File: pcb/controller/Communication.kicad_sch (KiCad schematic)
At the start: 4 parts, among them U2 SP3485EN, U3 E220-400M22S

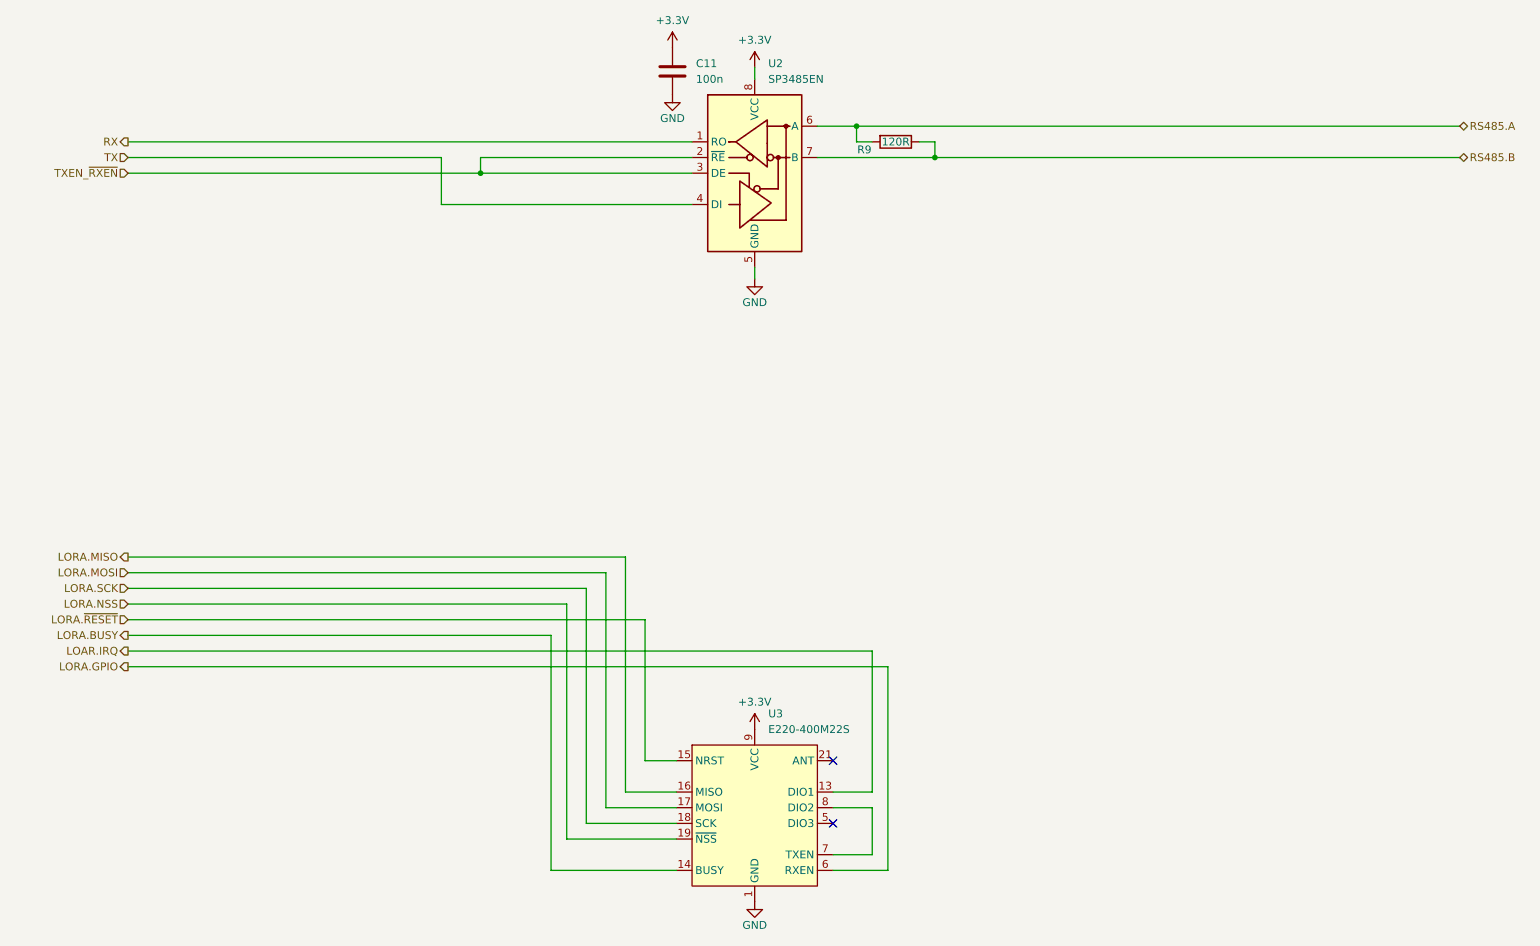
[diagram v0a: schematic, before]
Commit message: Revision 01 of Controller hardware
- fixed bugs from revision 00
- changed folder structure
- added ReleaseNotes_Controller.md to keep track of changes
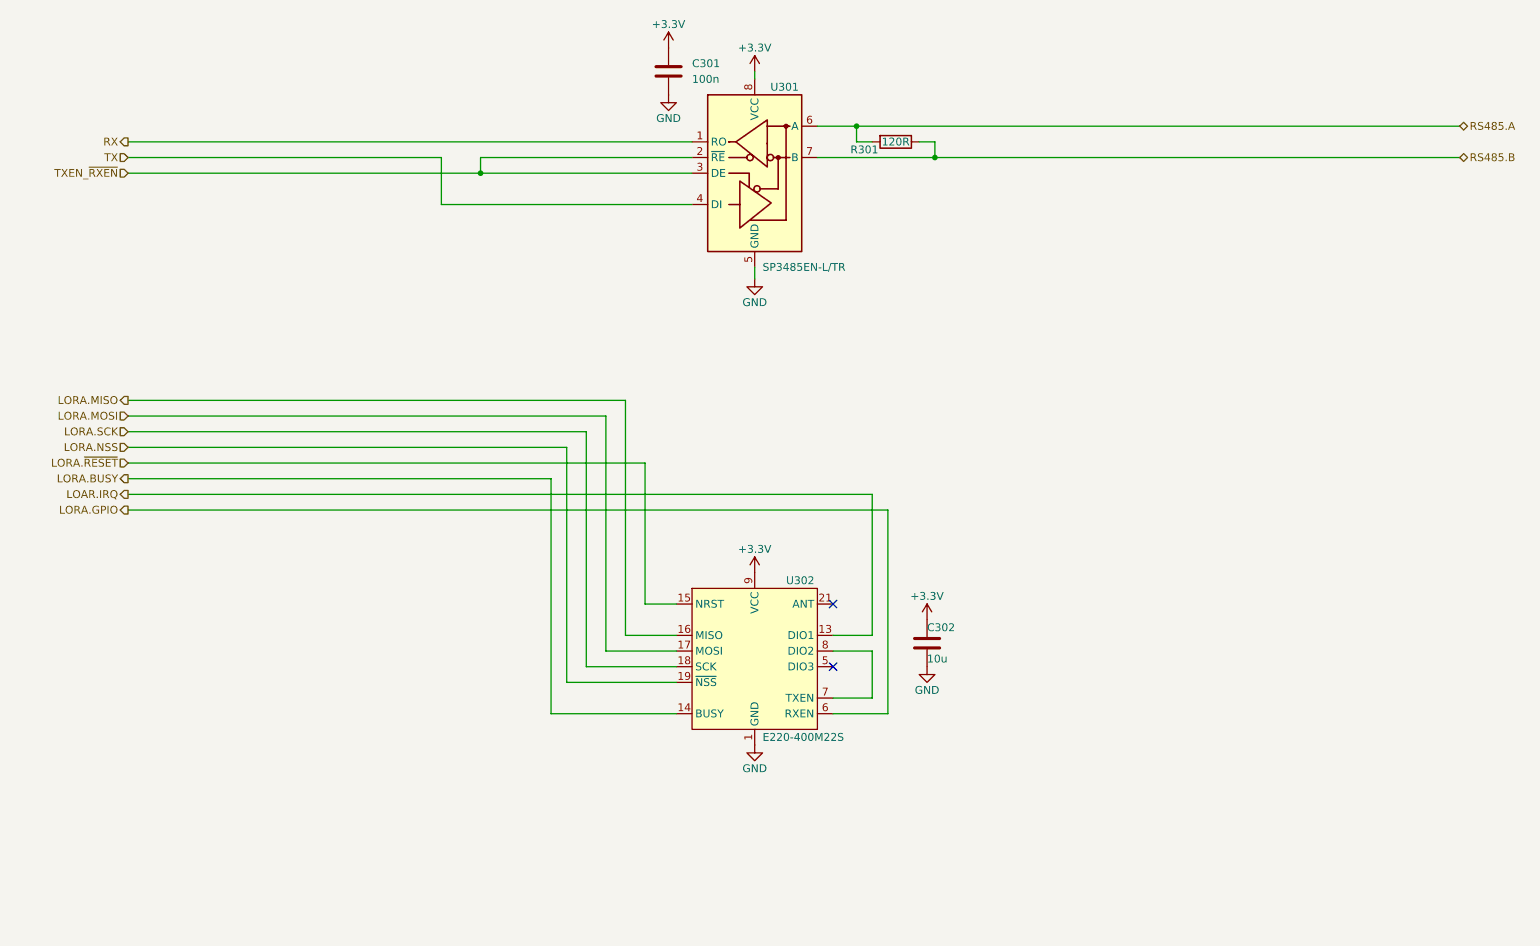
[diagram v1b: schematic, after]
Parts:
- added C302: 10u, Capacitor_SMD:C_0603_1608Metric, symbol Device:C
- C301: renamed from C11; LCSC Part # (none) -> C307331
- U301: renamed from U2; value SP3485EN -> SP3485EN-L/TR; LCSC Part # (none) -> C8963
- U302: renamed from U3; LCSC Part # (none) -> C2971737
- renumbered R9 to R301
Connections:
- net +3.3V: now also C302.1
- net GND: now also C302.2
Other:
- moved on the sheet: C301, U302
